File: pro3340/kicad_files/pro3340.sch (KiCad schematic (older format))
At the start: 89 parts, among them J1 HARD_SYNC, J10 PULSE, J11 SUB_PULSE, J2 SYNC, J3 LIN_FM, J4 1V/OCT, J5 EXP_FM, J6 PWM, J7 EURO_POWER, J8 TRIANGLE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

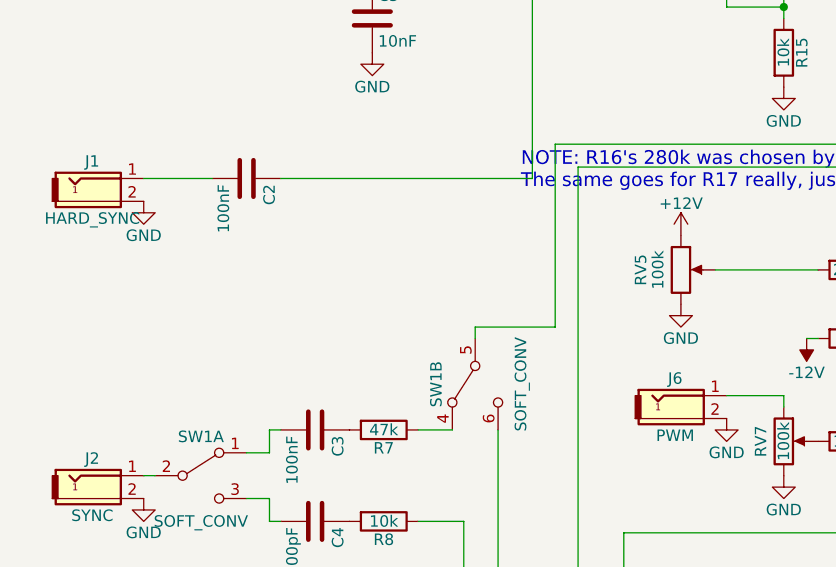
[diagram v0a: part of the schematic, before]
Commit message: Update 3340 schematic with notes
Also updating PDF, which wasn't the final version (at least the
power connector was wrong).
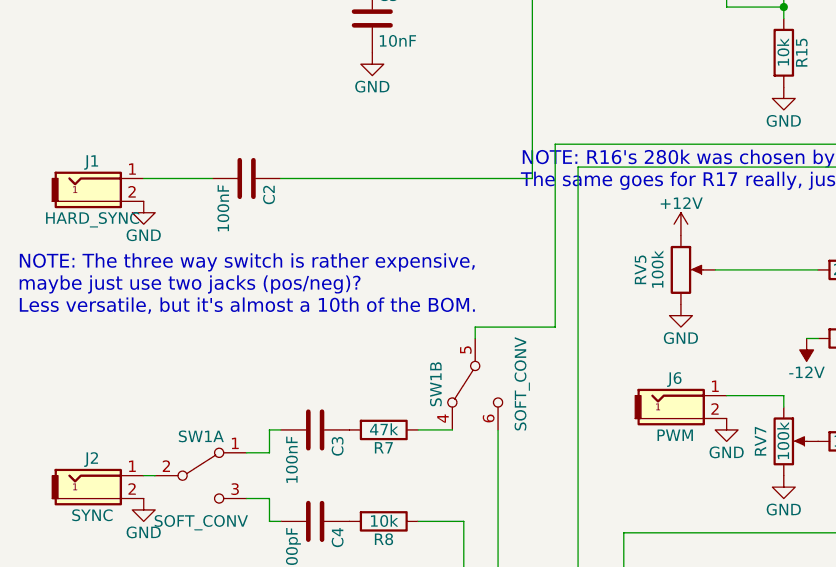
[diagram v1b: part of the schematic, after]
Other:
- note added: "NOTE: The three way switch is rather expensive, \nmaybe just use two jacks (pos/neg)? \nLess versatile, but it's almost a 10th of the BOM."
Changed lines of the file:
@@
 Text Notes 2750 4750 0    60   ~ 0
 NOTE: R16's 280k was chosen by tweaking a trimmer – theoretically maybe a lower value would be better. \nThe same goes for R17 really, just trimming in something to get better 0V out.
+Text Notes 550  5300 0    60   ~ 0
+NOTE: The three way switch is rather expensive, \nmaybe just use two jacks (pos/neg)? \nLess versatile, but it's almost a 10th of the BOM.
 $EndSCHEMATC
